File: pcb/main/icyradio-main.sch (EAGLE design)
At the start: 701 parts, among them CON101 FPC-22P, CON102 FPC-22P, CON1101 2EDG-2P-5MM-H, CON701 4P-SH-TOP, CON801 PCIE-X4-EDGE, J101 RJ45_MAG_LED_1G-TE-1-2301994-0, J701 TRSJACK, J702 TRSJACK, J703 TRSJACK, M701 SPH0641LM4H-1, M702 SPH0641LM4H-1, Q101 AO3400, Q102 AO3400, Q1101 AO3400, Q1102 AO4805, Q1103 AO3400, Q1104 AO4805, Q1105 AO4805, Q1106 AO3400, T501 UWB1-85E, T502 UWB1-85E, T503 UWB1-85E, T504 UWB1-85E, T505 UWB1-85E, T506 UWB1-85E, T507 UWB1-85E, T508 UWB1-85E, U1001 LTC4313-3, U1002 UPD301C, U1003 MIC2019, U101 MIC2019, U102 RPI-CM4, U1101 MCP1804-3302, U1102 LT7182S, U1201 ADM7172ACPZ-5.0, U1202 ADM7171ACPZ-1.3, U1203 ADM7171ACPZ-3.3, U1204 MIC23159, U1205 MIC5166, U1206 ADM7171ACPZ-1.3, U1207 ADM7171ACPZ-3.3, U1208 MIC23159, U1209 MIC23155, U1210 ADP7142AUJZ-3.3, U201 XC7A100TFGG484, U202 SST26VF064B, U301 MT41K256M16TW-125, U302 DSC1203DA3-333M3333, U401 AD9361, U501 MIC2019, U502 MIC2019, U503 MIC2019, U504 MIC2019, U505 ADL5601, U506 ADL5601, U601 8V97003, U701 ADAU1372, U901 DSB321SDA, U902 SI5351C-B-GM

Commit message: Silk screen done
Signed-off-by: João Silva <jgc3silva@gmail.com>
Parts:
- removed C1, C2: 100uF, Capacitor:CAPACITOR-0805
- removed C3, C4: 47uF, Capacitor:CAPACITOR-0603
- added C1258: 4.7uF, Capacitor:CAPACITOR-0603
- added C1259: 10uF, Capacitor:CAPACITOR-0402
- added C723, C724: 2.2uF, Capacitor:CAPACITOR-0402
- C1222: value 4.7uF -> 47uF; device Capacitor:CAPACITOR-0402 -> Capacitor:CAPACITOR-0603
- C1223: value 1uF -> 47uF; device Capacitor:CAPACITOR-0402 -> Capacitor:CAPACITOR-0603
- C1224: value 100nF -> 4.7uF
- C1225: value 100uF -> 1uF; device Capacitor:CAPACITOR-1206 -> Capacitor:CAPACITOR-0402
- C1227, C1254: value 100nF -> 100uF; device Capacitor:CAPACITOR-0402 -> Capacitor:CAPACITOR-1206
- C1229: value 10nF -> 100nF
- C1230, C1256: value 4.7uF -> 100nF; device Capacitor:CAPACITOR-0603 -> Capacitor:CAPACITOR-0402
- C1232: value 1uF -> 4.7uF; device Capacitor:CAPACITOR-0402 -> Capacitor:CAPACITOR-0603
- C1233: value 10uF -> 10nF
- C1234: value 10uF -> 1uF
- C1237, C1243: value 100nF -> 10uF
- C1239, C1253: value 10uF -> 100nF
- C1240: value 4.7uF -> 10uF; device Capacitor:CAPACITOR-0603 -> Capacitor:CAPACITOR-0402
- C1242: value 10uF -> 4.7uF; device Capacitor:CAPACITOR-0402 -> Capacitor:CAPACITOR-0603
- C1244: value 100uF -> 10uF; device Capacitor:CAPACITOR-1206 -> Capacitor:CAPACITOR-0402
- C1246: value 4.7uF -> 100uF; device Capacitor:CAPACITOR-0603 -> Capacitor:CAPACITOR-1206
- C1247, C1250: value 470pF -> 100nF
- C1248: value 100nF -> 4.7uF; device Capacitor:CAPACITOR-0402 -> Capacitor:CAPACITOR-0603
- C1251: value 100nF -> 470pF
- C1252: value 100uF -> 470pF; device Capacitor:CAPACITOR-1206 -> Capacitor:CAPACITOR-0402
- C712: value 100nF -> 100uF; device Capacitor:CAPACITOR-0402 -> Capacitor:CAPACITOR-0805
- C715: value 47uF -> 100uF; device Capacitor:CAPACITOR-0603 -> Capacitor:CAPACITOR-0805
- C716: value 47uF -> 100nF; device Capacitor:CAPACITOR-0603 -> Capacitor:CAPACITOR-0402
- C719, C720: value DNP -> 47uF; device Capacitor:CAPACITOR-0402 -> Capacitor:CAPACITOR-0603
- C721, C722: value 2.2uF -> DNP
- renumbered FB1 to FB301
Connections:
- net 0V675_DDR3_VREF: now also C1234.C1; no longer C1232.C1
- net 0V675_DDR3_VTT: now also C1235.C1, C1238.C1; no longer C1233.C1, C1236.C1
- net 1V2: now also C1259.C1; no longer C1255.C1
- net 1V2_SS: now also C1251.C1; no longer C1249.C1
- net 1V35: now also C1224.C1; no longer C1222.C1
- net 1V3_TRX: now also C1236.C1, C1240.C1, C1243.C1, C1244.C1; no longer C1234.C1, C1238.C1, C1241.C1, C1242.C1
- net 1V8: now also C1226.C1, C1227.C1; no longer C1224.C1, C1225.C1
- net 2V5: now also C1222.C1, C1228.C1, C1245.C1, C1246.C1; no longer C1226.C1, C1243.C1, C1244.C1, C4.C1
- net 2V5_SS: now also C1249.C1; no longer C1247.C1
- net 3V3: now also C1253.C1, C1254.C1; no longer C1251.C1, C1252.C1
- net 3V3_CODEC: now also C1255.C1, C716.C1; no longer C1253.C1, C712.C1
- net 3V3_SS: now also C1252.C1; no longer C1250.C1
- net 3V3_SYNTH_VCO_RF: now also C1237.C1, C1241.C1; no longer C1235.C1, C1239.C1
- net 5V0: now also C1225.C1, C1229.C1, C1232.C1, C1239.C1, C1242.C1, C1247.C1, C1250.C1, C1258.C1; no longer C1227.C1, C1228.C1, C1237.C1, C1240.C1, C1245.C1, C1246.C1, C1254.C1, C3.C1
- net CODEC_LINE_IN_L: now also C719.C1; no longer C717.C1
- net CODEC_LINE_IN_R: now also C720.C1; no longer C718.C1
- net CODEC_MICBIAS0: now also C723.C1; no longer C721.C1
- net CODEC_MICBIAS1: now also C724.C1; no longer C722.C1
- net CODEC_MIC_IN_L: now also C717.C1; no longer C715.C1
- net CODEC_MIC_IN_R: now also C718.C1; no longer C716.C1
- net CODEC_OUT_L: now also C712.C1; no longer C2.C1
- net CODEC_OUT_R: now also C715.C1; no longer C1.C1
- net GND: now also C1258.C2, C1259.C2, C716.C2, C723.C2, C724.C2; no longer C3.C2, C4.C2, C712.C2, C719.C2, C720.C2
- net N$38: now also C718.C2; no longer C716.C2
- net N$39: now also C717.C2; no longer C715.C2
- net N$42: now also C715.C2; no longer C1.C2
- net N$44: now also C712.C2; no longer C2.C2
- net N$5: now also C1231.C1; no longer C1229.C1
- net N$55: now also C721.C1; no longer C719.C1
- net N$56: now also C722.C1; no longer C720.C1
- net N$7: now also C720.C2; no longer C718.C2
- net N$9: now also C719.C2; no longer C717.C2
- net N$97: now also C1233.C1; no longer C1231.C1
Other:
- moved on the sheet: C1222, C1223, C1224, C1225, C1226, C1227, C1228, C1229, C1230, C1231, C1232, C1233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

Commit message: Minor updates
Signed-off-by: João Silva <jgc3silva@gmail.com>
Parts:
- added C909: 100nF, Capacitor:CAPACITOR-0402
- C615, C903: value 100nF -> 1uF
- C621, C622: value 10nF -> 10pF
- C623, C624, C625, C626: value 100nF -> 20pF
- C905: value 10pF -> 100nF
- C907: value 100nF -> 10pF
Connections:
- net 3V3_CLK_MNGR: now also C905.C1, C909.C1; no longer C907.C1
- net CLK_MNGR_REF_ACC: now also C907.C2; no longer C906.C2
- net CLK_MNGR_REF_DCC: now also C907.C1; no longer C905.C1
- net GND: now also C906.C2, C909.C2; no longer C907.C2
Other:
- moved on the sheet: C902, C903, C904, C905, C906, C907, C908, FB901

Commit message: Minor changes
Signed-off-by: João Silva <jgc3silva@gmail.com>
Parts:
- added C333, C334: 47uF, Capacitor:CAPACITOR-0603
- C323: value 1uF -> 10uF; device Capacitor:CAPACITOR-0402 -> Capacitor:CAPACITOR-0603
- C324: value 100nF -> 1uF
- C325: value 100nF -> 10nF
- C329, C330: value 4.7uF -> 100nF
- C331, C332: value 47uF -> 4.7uF; device Capacitor:CAPACITOR-0603 -> Capacitor:CAPACITOR-0402
- R325: value 40.2 Ohms -> DNP
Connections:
- net 0V675_DDR3_VTT: now also C326.C2, C333.C1, C334.C1; no longer C324.C2, C325.C1, C326.C1
- net 3V3: now also C323.C1
- net 3V3_DDR3_CLK: now also C324.C1, C325.C1; no longer C323.C1
- net GND: now also C324.C2, C333.C2, C334.C2; no longer C326.C2
- net N$87: now also C326.C1; no longer C324.C1
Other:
- moved on the sheet: C323, C324, C325, C326, C327, C328, C329, C330, C331, C332, FB301, R302

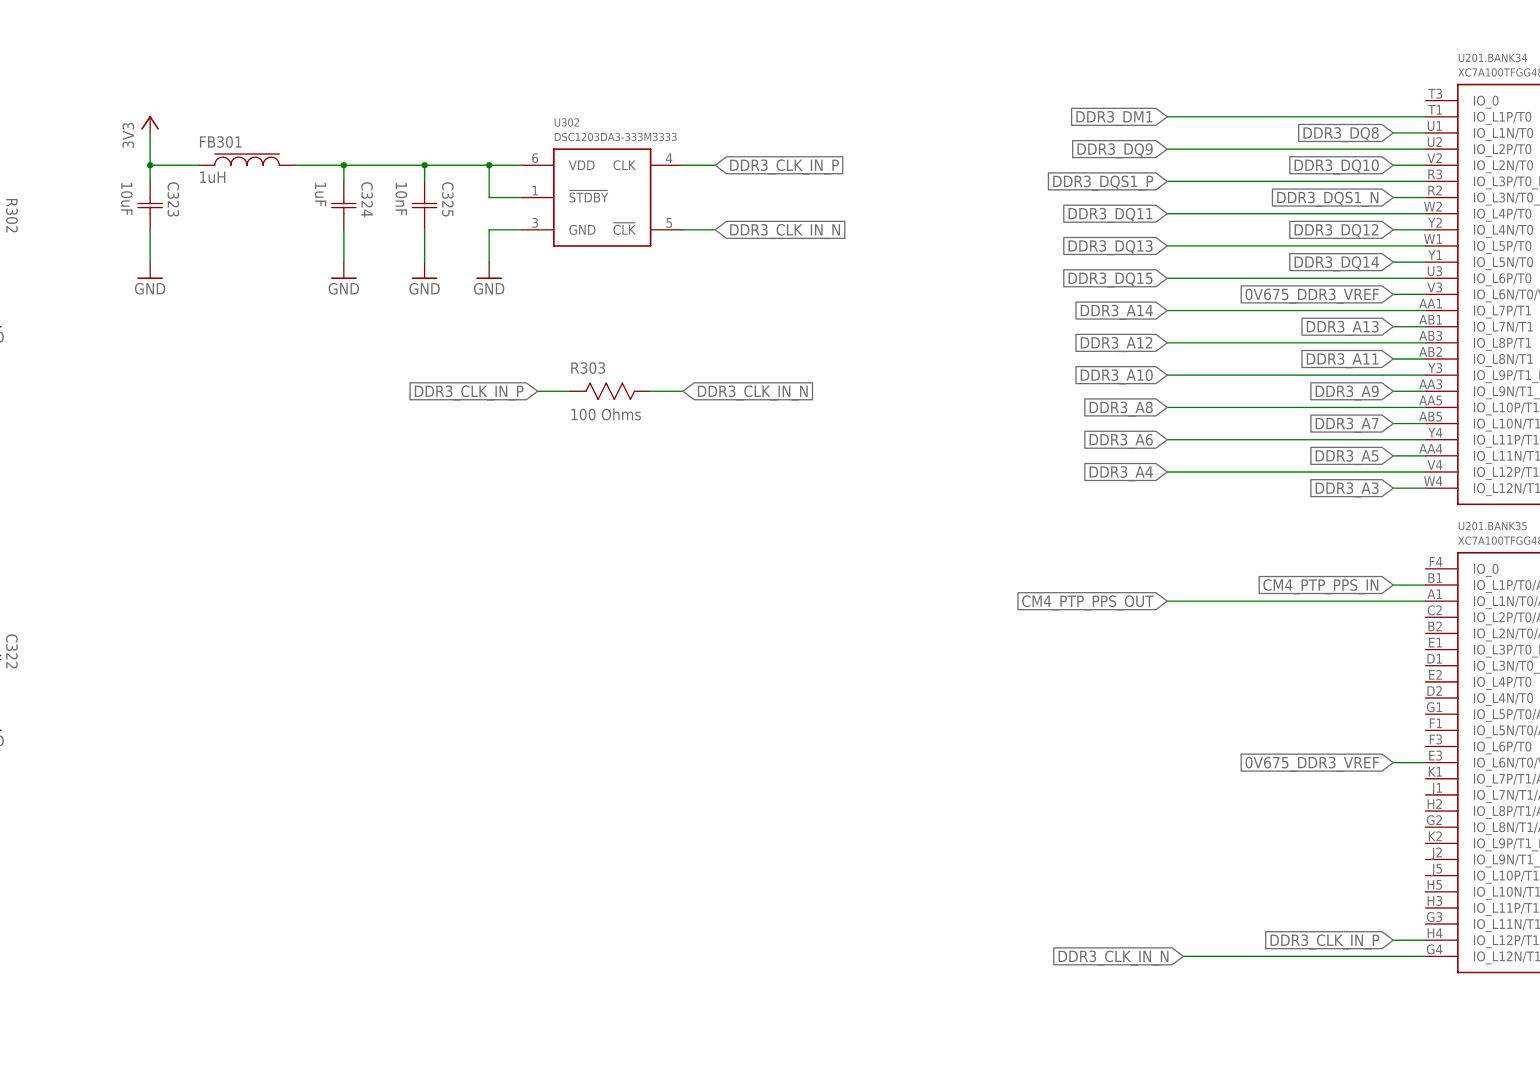
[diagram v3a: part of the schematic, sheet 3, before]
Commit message: Remove dedicated DDR3 oscillator
Signed-off-by: João Silva <jgc3silva@gmail.com>
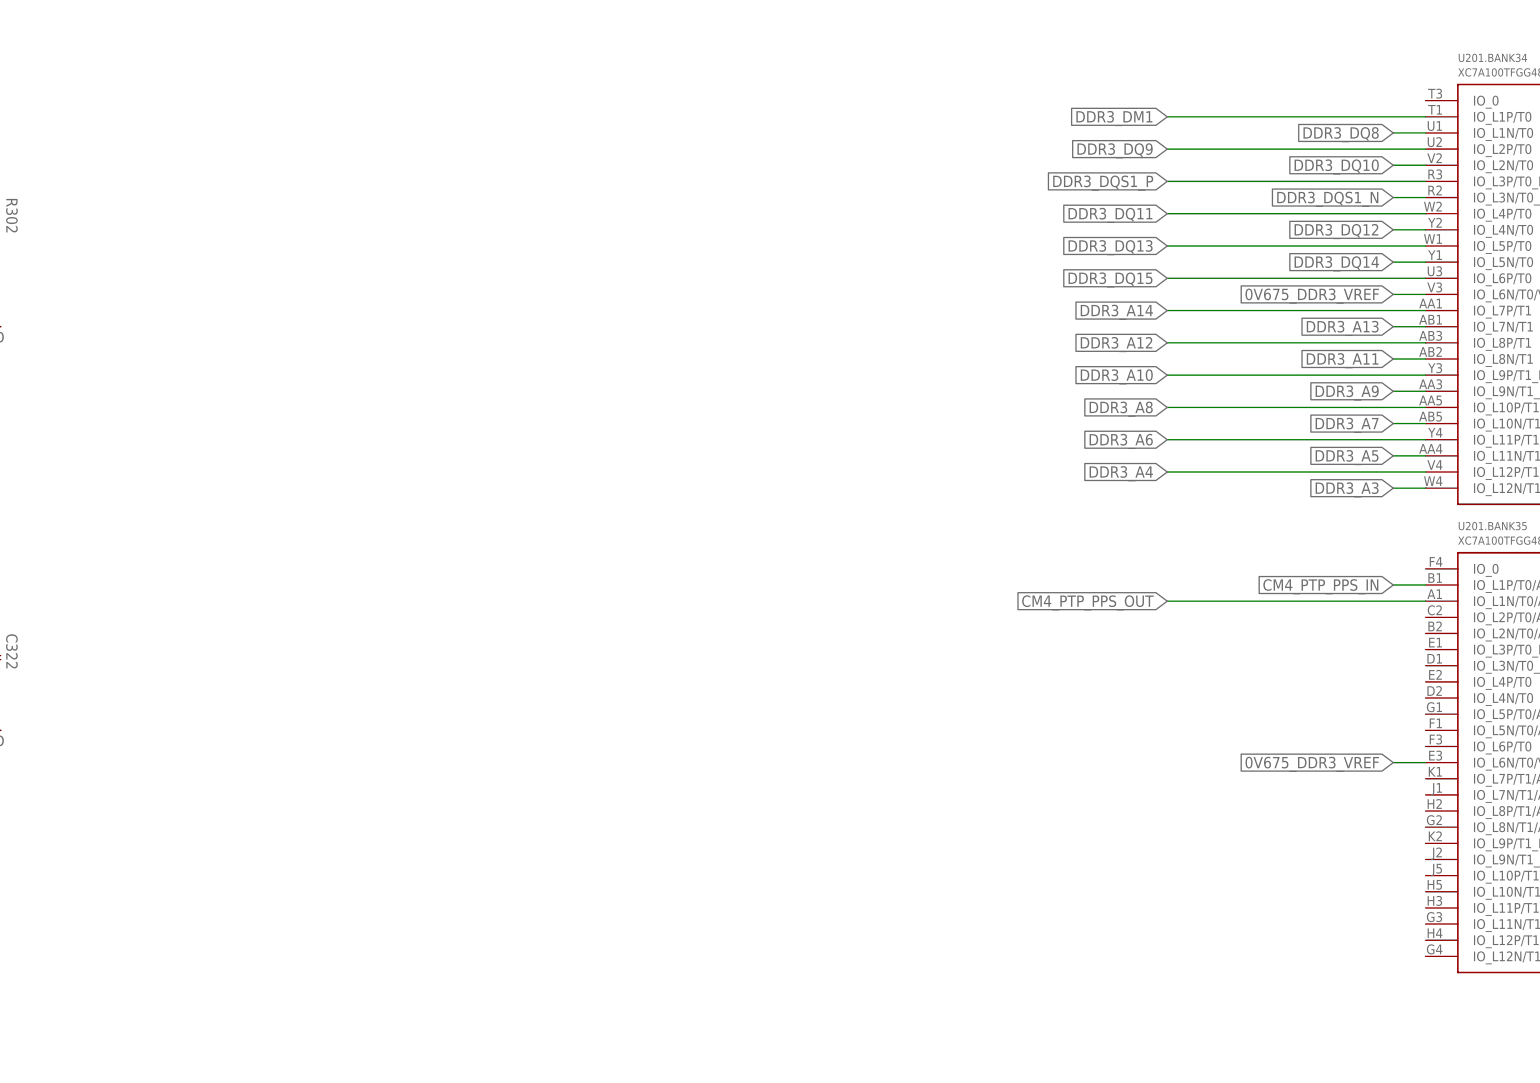
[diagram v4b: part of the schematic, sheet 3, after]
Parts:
- removed C323: 10uF, Capacitor:CAPACITOR-0603
- removed C324: 1uF, Capacitor:CAPACITOR-0402
- removed C325: 10nF, Capacitor:CAPACITOR-0402
- removed FB301: 1uH, Inductor:FERRITE-0603
- removed R303: 100 Ohms, Resistor:RESISTOR-0402
- removed U302: DSC1203DA3-333M3333, Microchip:DSC1203DA3-333M3333
- C708: value 100nF -> 1uF
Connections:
- removed net 3V3_DDR3_CLK: C324.C1, C325.C1, FB301.2, U302.!STDBY, U302.VDD
- removed net DDR3_CLK_IN_N: R303.1, U201.BANK35.IO_L12N/T1/MRCC, U302.!CLK
- removed net DDR3_CLK_IN_P: R303.2, U201.BANK35.IO_L12P/T1/MRCC, U302.CLK
- net 3V3: no longer C323.C1, FB301.1
- net GND: no longer C323.C2, C324.C2, C325.C2, U302.GND

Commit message: Finish checklist and generate gerbers
Signed-off-by: João Silva <jgc3silva@gmail.com>
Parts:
- removed C332: 4.7uF, Capacitor:CAPACITOR-0402
- removed C333, C334: 47uF, Capacitor:CAPACITOR-0603
- removed R329: 40.2 Ohms, Resistor:RESISTOR-0402
- added C323, C324, C325: 100nF, Capacitor:CAPACITOR-0402
- added R120, R121: 2.2K Ohms, Resistor:RESISTOR-0402
- added R303: 40.2 Ohms, Resistor:RESISTOR-0402
- C328, C329: value 100nF -> 4.7uF
- C330: value 100nF -> 47uF; device Capacitor:CAPACITOR-0402 -> Capacitor:CAPACITOR-0603
- C331: value 4.7uF -> 47uF; device Capacitor:CAPACITOR-0402 -> Capacitor:CAPACITOR-0603
- R110: value 1K Ohms -> DNP
- R112: value 220 Ohms -> DNP
- R113: value 220 Ohms -> 1K Ohms
- R118, R119: value 2.2K Ohms -> 220 Ohms
- R324: value 40.2 Ohms -> DNP
- R325: value DNP -> 40.2 Ohms
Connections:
- net !DDR3_CAS: now also R327.1; no longer R328.1
- net !DDR3_RAS: now also R323.1; no longer R324.1
- net !DDR3_RESET: now also R324.1; no longer R325.1
- net !DDR3_WE: now also R322.1; no longer R323.1
- net 0V675_DDR3_VTT: now also C323.C2, C324.C1, C325.C1, C326.C1, R303.1, R312.1, R320.2; no longer C326.C2, C332.C1, C333.C1, C334.C1, R311.1, R319.1, R329.2
- net 3V3_CM4: now also R120.2, R121.2; no longer R112.2, R113.2
- net CM4_CAM1_SCL: now also R121.1; no longer R119.1
- net CM4_CAM1_SDA: now also R120.1; no longer R118.1
- net CM4_PTP_PPS_IN: now also R110.2
- net CM4_PTP_PPS_OUT: now also R112.2, R113.2; no longer R110.2
- net DDR3_A0: now also R303.2; no longer R304.2
- net DDR3_A1: now also R312.2; no longer R313.2
- net DDR3_A10: now also R308.2; no longer R309.2
- net DDR3_A11: now also R317.2; no longer R318.2
- net DDR3_A12: now also R309.2; no longer R310.2
- net DDR3_A13: now also R318.2; no longer R319.2
- net DDR3_A14: now also R310.2; no longer R311.2
- net DDR3_A2: now also R304.2; no longer R305.2
- net DDR3_A3: now also R313.2; no longer R314.2
- net DDR3_A4: now also R305.2; no longer R306.2
- net DDR3_A5: now also R314.2; no longer R315.2
- net DDR3_A6: now also R306.2; no longer R307.2
- net DDR3_A7: now also R315.2; no longer R316.2
- net DDR3_A8: now also R307.2; no longer R308.2
- net DDR3_A9: now also R316.2; no longer R317.2
- net DDR3_BA0: now also R321.1; no longer R322.1
- net DDR3_BA1: now also R325.1; no longer R326.1
- net DDR3_BA2: now also R320.1; no longer R321.1
- net DDR3_CLK_EN: now also R328.1; no longer R329.1
- net DDR3_CLK_N: now also R319.1; no longer R320.1
- net DDR3_CLK_P: now also R311.2; no longer R312.2
- net DDR3_ODT: now also R326.1; no longer R327.1
- net ETH_SYNC_OUT: now also R113.1; no longer R110.1
- net GND: now also C324.C2, C325.C2, C326.C2, R110.1, R112.1, U401.RF.AUXADC; no longer C332.C2, C333.C2, C334.C2
- net N$48: now also R119.1; no longer R113.1
- net N$50: now also R118.1; no longer R112.1
- net N$87: now also C323.C1, R311.1, R319.2; no longer C326.C1, R312.1, R320.2
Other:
- note removed: "TODO: - AUXDAC - AUXADC - Add keepout on RF components"
- note removed: "TODO: - Review current requirements - Check if the parts can supply the requested current"
- moved on the sheet: C101, C105, C107, C326, C327, C328, C329, C330, C331, J101.GREEN, J101.PORT, J101.YELLOW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

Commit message: Some PCB rectifications and removal of old gerbers
Signed-off-by: João Silva <jgc3silva@gmail.com>
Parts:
- added C263: 4.7uF, Capacitor:CAPACITOR-0402
- added C264: 100nF, Capacitor:CAPACITOR-0402
- C256: value 100nF -> 47uF; device Capacitor:CAPACITOR-0402 -> Capacitor:CAPACITOR-0603
- C257: value 4.7uF -> 47uF; device Capacitor:CAPACITOR-0402 -> Capacitor:CAPACITOR-0603
- C260: value 100nF -> 4.7uF
- C261: value 4.7uF -> 100nF
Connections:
- net 1V0: now also C262.C1, C263.C1; no longer C260.C1
- net 1V2: now also C257.C1
- net 1V35: now also C260.C1; no longer C259.C1
- net 2V5: now also C259.C1; no longer C258.C1
- net 3V3: now also C258.C1, C264.C1; no longer C257.C1, C262.C1
- net GND: now also C263.C2, C264.C2
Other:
- moved on the sheet: C256, C257, C258, C259, C260, C261, C262
